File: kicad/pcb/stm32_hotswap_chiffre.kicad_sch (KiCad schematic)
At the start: 23 parts, among them J1 USB_C_Receptacle_USB2.0, J2 OLED I2C, U1 STM32F072CBT6, U2 PRTR5V0U2X

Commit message: v0.2.2
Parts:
- SW?: footprint modified_footrprints:SW_SPST_SKQG_WithoutStem -> modified_footprints:SW_SPST_SKQG_WithoutStem
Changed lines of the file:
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@@
       (effects (font (size 1.27 1.27)))
     )
-    (property "Footprint" "modified_footrprints:SW_SPST_SKQG_WithoutStem" (at 83.82 62.23 0)
+    (property "Footprint" "modified_footprints:SW_SPST_SKQG_WithoutStem" (at 83.82 62.23 0)
       (effects (font (size 1.27 1.27)) hide)
     )

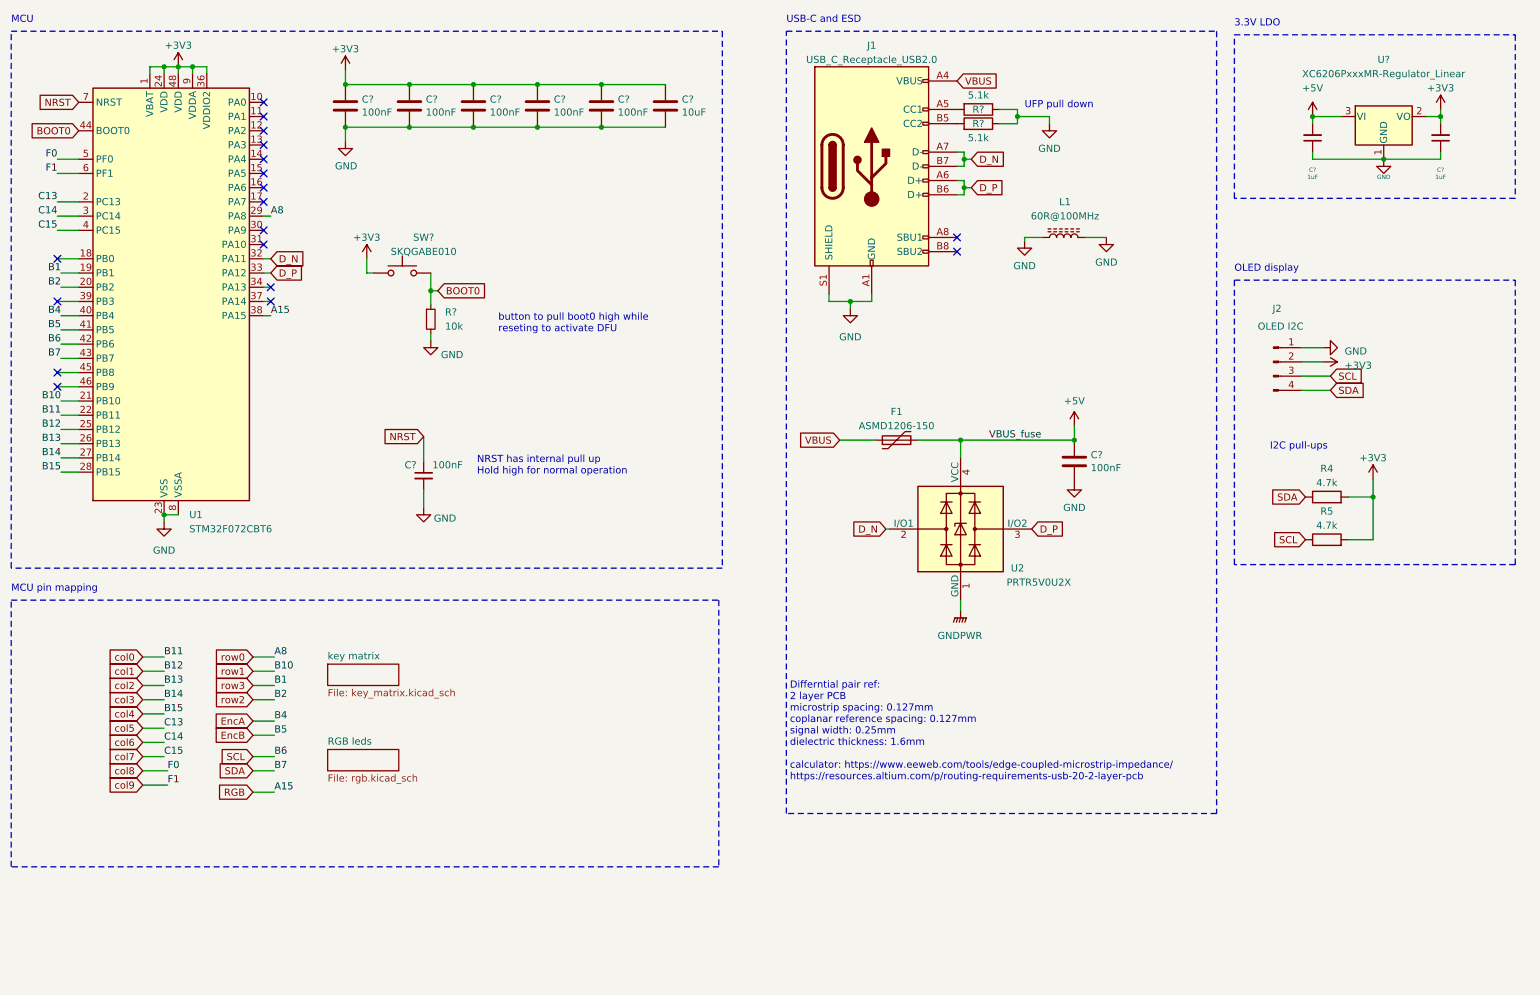
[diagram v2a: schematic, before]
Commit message: Initial SAM/nRF52 version.
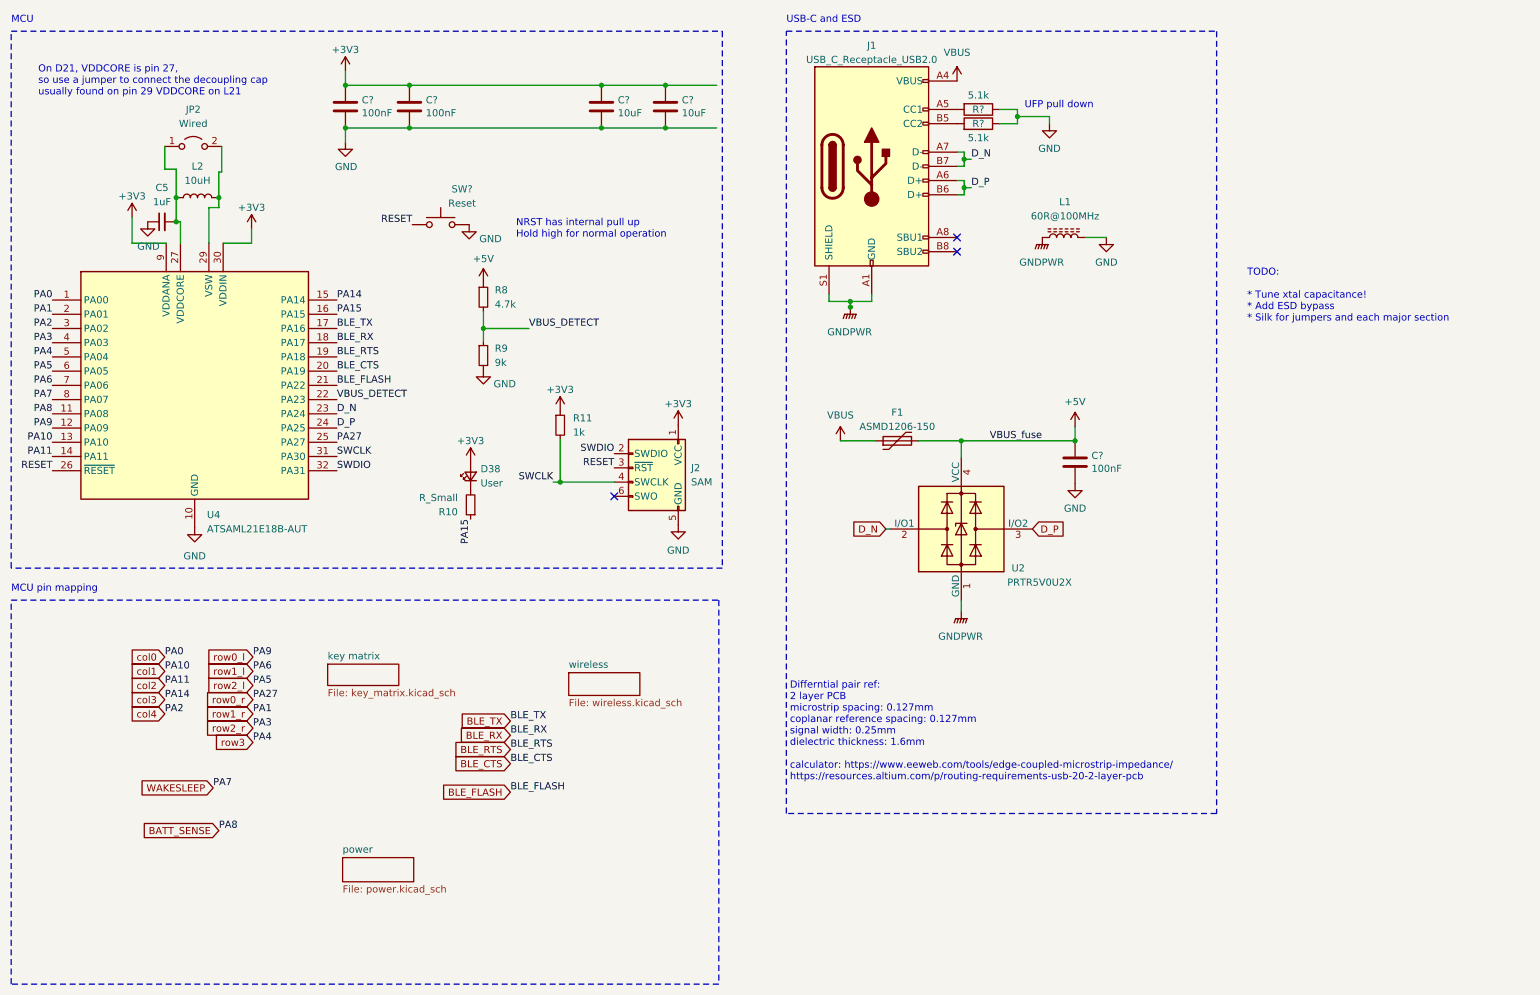
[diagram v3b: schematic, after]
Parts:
- removed C? (x2): 1uF, Capacitor_SMD:C_0402_1005Metric, symbol Device:C_Small
- removed C? (x2): 100nF, Capacitor_SMD:C_0402_1005Metric, symbol Device:C
- removed C?: 100nF, Capacitor_SMD:C_0402_1005Metric, symbol Device:C_Small
- removed J2: OLED I2C, Connector_PinHeader_2.54mm:PinHeader_1x04_P2.54mm_Vertical, symbol Connector:Conn_01x04_Pin
- removed R4, R5: 4.7k, Resistor_SMD:R_0402_1005Metric, symbol Device:R
- removed R?: 10k, Resistor_SMD:R_0402_1005Metric, symbol Device:R_Small
- removed U1: STM32F072CBT6, Package_QFP:LQFP-48_7x7mm_P0.5mm, symbol MCU_ST_STM32F0:STM32F072CBTx
- removed U?: XC6206PxxxMR-Regulator_Linear, Package_TO_SOT_SMD:SOT-23, symbol kicad-keyboard-parts:XC6206PxxxMR-Regulator_Linear
- added C5: 1uF, Capacitor_SMD:C_0805_2012Metric, symbol Device:C_Small
- added D38: User, LED_SMD:LED_0805_2012Metric, symbol Device:LED_Small
- added J2: SAM, PCM_marbastlib-various:CON_TC2030_outlined, symbol PCM_marbastlib-various:TC2030_SWD
- added JP2: Wired, Jumper:SolderJumper-2_P1.3mm_Open_TrianglePad1.0x1.5mm, symbol Jumper:Jumper_2_Open
- added L2: 10uH, Inductor_SMD:L_0805_2012Metric, symbol Device:L
- added R10: R_Small, Resistor_SMD:R_0805_2012Metric, symbol Device:R_Small
- added R11: 1k, Resistor_SMD:R_0805_2012Metric, symbol Device:R_Small
- added R8: 4.7k, Resistor_SMD:R_0805_2012Metric, symbol Device:R_Small
- added R9: 9k, Resistor_SMD:R_0805_2012Metric, symbol Device:R_Small
- added U4: ATSAML21E18B-AUT, Package_QFP:TQFP-32_7x7mm_P0.8mm, symbol MCU_Microchip_SAML:ATSAML21E18B-AUT
- C? (x3): footprint Capacitor_SMD:C_0402_1005Metric -> Capacitor_SMD:C_0805_2012Metric
- C?: footprint Capacitor_SMD:C_0603_1608Metric -> Capacitor_SMD:C_0805_2012Metric
- C?: value 100nF -> 10uF; footprint Capacitor_SMD:C_0402_1005Metric -> Capacitor_SMD:C_0805_2012Metric
- R? (x2): footprint Resistor_SMD:R_0402_1005Metric -> Resistor_SMD:R_0805_2012Metric
- SW?: value SKQGABE010 -> Reset; MPN (none) -> SKQGABE010
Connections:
- net BOOT0 is gone; now on net GND: SW?.2
- net +3V3: now also D38.2 (A), J2.1 (VCC), R11.1, U4.30 (VDDIN), U4.9 (VDDANA); no longer SW?.1
- net +5V: now also R8.1
- net D_N: now also U4.23 (PA24)
- net D_P: now also U4.24 (PA25)
- net GND: now also C5.1, J2.5 (GND), R9.2, U4.10 (GND), U4.28 (GND); no longer J1.A1 (GND), J1.A12 (GND), J1.B1 (GND), J1.B12 (GND), J1.S1 (SHIELD), L1.1
- net GNDPWR: now also J1.A1 (GND), J1.A12 (GND), J1.B1 (GND), J1.B12 (GND), J1.S1 (SHIELD), L1.1
- net col0: now also U4.1 (PA00)
- net col1: now also U4.13 (PA10)
- net col2: now also U4.14 (PA11)
- net col3: now also U4.15 (PA14)
- net col4: now also U4.3 (PA02)
- net row3: now also U4.5 (PA04)
- new net: D38.1 (K), R10.2
- new net: C5.2, JP2.1 (A), L2.1, U4.27 (VDDCORE)
- new net: JP2.2 (B), L2.2, U4.29 (VSW)
- new net BATT_SENSE: U4.11 (PA08)
- new net BLE_CTS: U4.20 (PA19)
- new net BLE_FLASH: U4.21 (PA22)
- new net BLE_RTS: U4.19 (PA18)
- new net BLE_RX: U4.18 (PA17)
- new net BLE_TX: U4.17 (PA16)
- new net PA15: R10.1, U4.16 (PA15)
- new net RESET: J2.3 (~{RST}), SW?.1, U4.26 (~{RESET})
- new net SWCLK: J2.4 (SWCLK), R11.2, U4.31 (PA30)
- new net SWDIO: J2.2 (SWDIO), U4.32 (PA31)
- new net VBUS_DETECT: R8.2, R9.1, U4.22 (PA23)
- new net WAKESLEEP: U4.8 (PA07)
- new net row0_l: U4.12 (PA09)
- new net row0_r: U4.25 (PA27)
- new net row1_l: U4.7 (PA06)
- new net row1_r: U4.2 (PA01)
- new net row2_l: U4.6 (PA05)
- new net row2_r: U4.4 (PA03)
- no-connect marks 18 -> 3
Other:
- removed sheet RGB leds
- added sheet power (power.kicad_sch)
- added sheet wireless (wireless.kicad_sch)
- note added: "On D21, VDDCORE is pin 27, so use a jumper to connect the decoupling cap usually found on pin 29 VDDCORE on L21"
- note added: "TODO: * Tune xtal capacitance! * Add ESD bypass * Silk for jumpers and each major section"
- note removed: "3.3V LDO"
- note removed: "I2C pull-ups"
- note removed: "OLED display"
- note removed: "button to pull boot0 high while reseting to activate DFU"
- moved on the sheet: SW?
